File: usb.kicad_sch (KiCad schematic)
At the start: 23 parts, among them J26 FTSH-105-01-L-DV-K, J3 CX90B1-24P, U3 MSPM0G5187SPMR, U8 TPD4E004DRYR, Y4 32.768KHz 12.5pF 20ppm

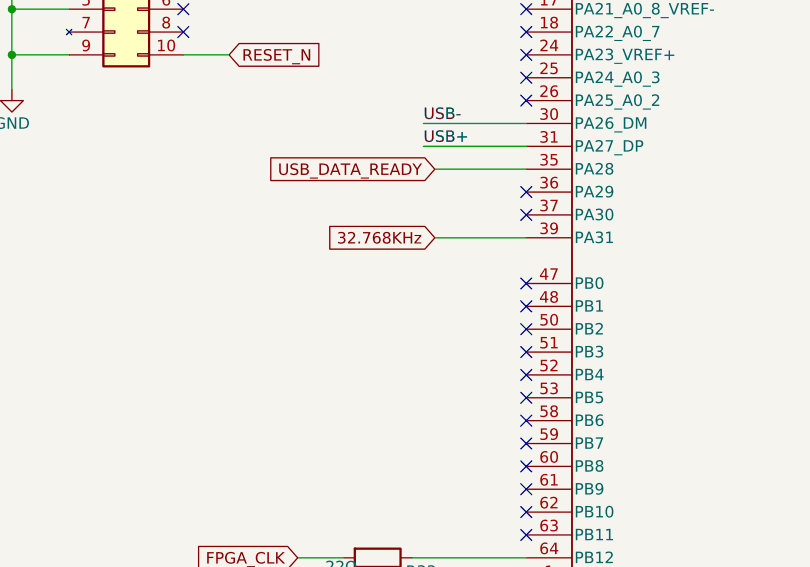
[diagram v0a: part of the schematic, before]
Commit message: Split the USB CPU and main CPU reset lines
Signed-off-by: Corey Minyard <corey@minyard.net>
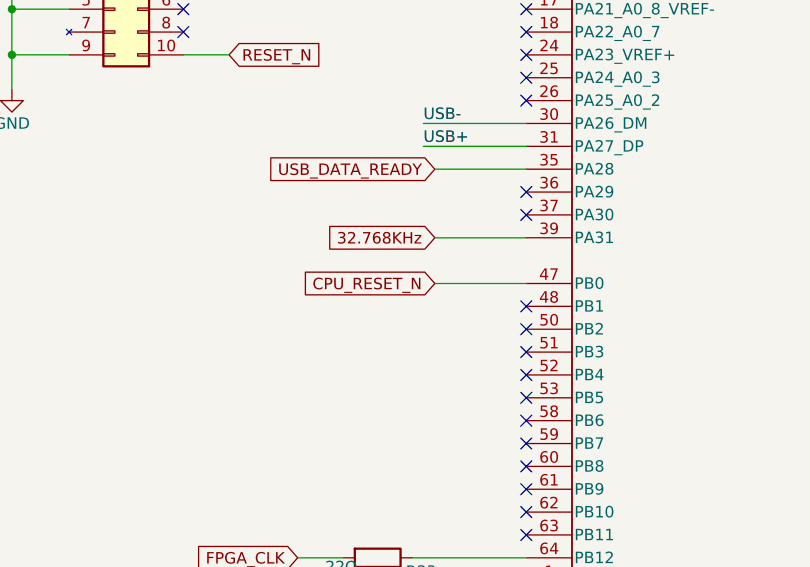
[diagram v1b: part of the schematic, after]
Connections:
- net CPU_RESET_N: now reaches U3.47 (PB0)
- no-connect marks 55 -> 54
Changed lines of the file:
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@@
-	)
-	(no_connect
-		(at 95.25 124.46)
 	)
 	(no_connect
@@
 		(pts
 			(xy 191.77 67.31) (xy 194.31 67.31)
+		)
+		(stroke
+			(width 0)
+			(type default)
+		)
+	)
+	(wire
+		(pts
+			(xy 85.09 124.46) (xy 95.25 124.46)
 		)
 		(stroke
@@
 			(effects
 				(font
+					(size 1.27 1.27)
+				)
+				(justify right)
+				(hide yes)
+			)
+		)
+	)
+	(global_label "CPU_RESET_N"
+		(shape input)
+		(at 85.09 124.46 180)
+		(fields_autoplaced yes)
+		(effects
+			(font
+				(size 1.27 1.27)
+			)
+			(justify right)
+		)
+		(property "Intersheetrefs" "${INTERSHEET_REFS}"
+			(at 69.2235 124.46 0)
+			(effects
+				(font

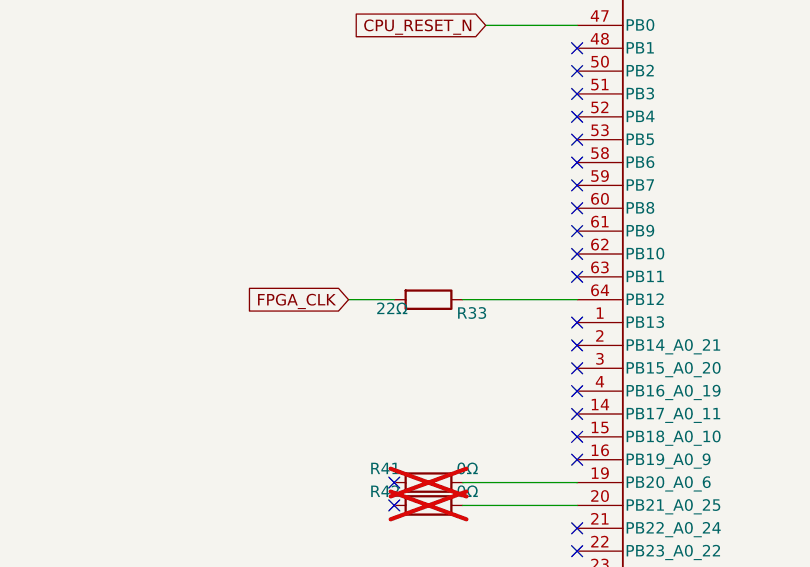
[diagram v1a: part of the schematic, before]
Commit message: Move he FPGA clock to pin 62 on the USB chip
That is easily drivable with PWM, if I can figure out how that works.

Signed-off-by: Corey Minyard <corey@minyard.net>
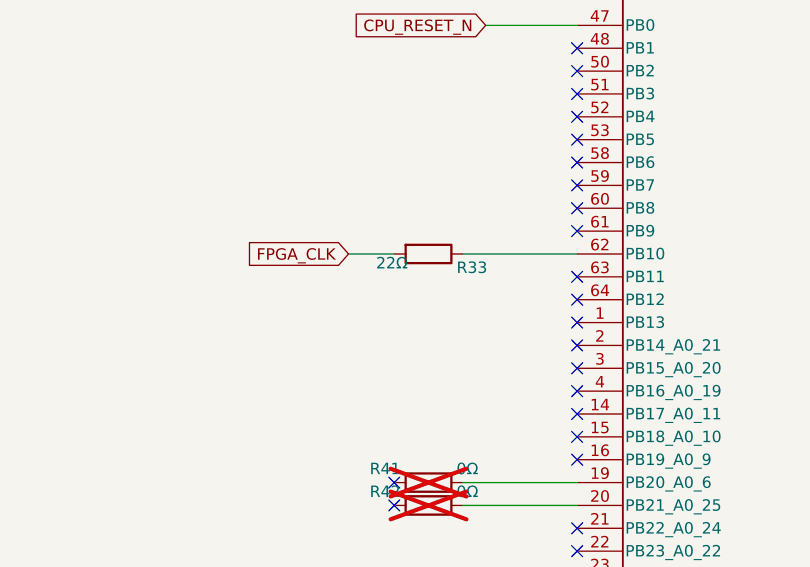
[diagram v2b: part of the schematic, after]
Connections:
- net at R33.1: now also U3.62 (PB10); no longer U3.64 (PB12)
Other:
- moved on the sheet: R33
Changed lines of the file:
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@@
+	)
+	(no_connect
+		(at 95.25 154.94)
 	)
 	(no_connect
@@
 	)
 	(no_connect
-		(at 95.25 149.86)
-	)
-	(no_connect
 		(at 95.25 137.16)
 	)
@@
 	(wire
 		(pts
+			(xy 82.55 149.86) (xy 95.25 149.86)
+		)
+		(stroke
+			(width 0)
+			(type default)
+		)
+	)
+	(wire
+		(pts
 			(xy 248.92 106.68) (xy 182.88 106.68)
 		)
@@
 	(wire
 		(pts
-			(xy 69.85 154.94) (xy 74.93 154.94)
-		)
-		(stroke
-			(width 0)
-			(type default)
-		)
-	)
-	(wire
-		(pts
 			(xy 238.76 85.09) (xy 257.81 85.09)
 		)
@@
 	(wire
 		(pts
+			(xy 69.85 149.86) (xy 74.93 149.86)
+		)
+		(stroke
+			(width 0)
+			(type default)
+		)
+	)
+	(wire
+		(pts
 			(xy 68.58 33.02) (xy 68.58 25.4)
 		)
@@
 		(pts
 			(xy 95.25 50.8) (xy 41.91 50.8)
-		)
-		(stroke
-			(width 0)
-			(type default)
-		)
-	)
-	(wire
-		(pts
-			(xy 82.55 154.94) (xy 95.25 154.94)
 		)
 		(stroke
@@
 		)
 	)
-	(global_label "FPGA_CLK"
-		(shape input)
-		(at 69.85 154.94 180)
-		(fields_autoplaced yes)
-		(effects
-			(font
-				(size 1.27 1.27)
-			)
-			(justify right)
-		)
-		(property "Intersheetrefs" "${INTERSHEET_REFS}"
-			(at 57.6119 154.94 0)
-			(effects
-				(font
-					(size 1.27 1.27)
-				)
-				(justify right)
-				(hide yes)
-			)
-		)
-	)
 	(global_label "USB_VBUS"
 		(shape input)
@@
 		(property "Intersheetrefs" "${INTERSHEET_REFS}"
 			(at 66.0786 111.76 0)
+			(effects
+				(font
+					(size 1.27 1.27)
+				)
+				(justify right)
+				(hide yes)
+			)
+		)
+	)
+	(global_label "FPGA_CLK"
+		(shape input)
+		(at 69.85 149.86 180)
+		(fields_autoplaced yes)
+		(effects
+			(font
+				(size 1.27 1.27)
+			)
+			(justify right)
+		)
+		(property "Intersheetrefs" "${INTERSHEET_REFS}"
+			(at 57.6119 149.86 0)
 			(effects
 				(font
@@
 	(symbol
 		(lib_id "Device:R")
-		(at 78.74 154.94 270)
+		(at 78.74 149.86 270)
 		(unit 1)
 		(exclude_from_sim no)
@@
 		(dnp no)
 		(property "Reference" "R33"
-			(at 83.566 156.464 90)
+			(at 83.566 151.384 90)
 			(effects
 				(font
@@
 		)
 		(property "Value" "22Ω"
-			(at 74.676 155.956 90)
+			(at 74.676 150.876 90)
 			(effects
 				(font
@@
 		)
 		(property "Footprint" "Resistor_SMD:R_0402_1005Metric_Pad0.72x0.64mm_HandSolder"
-			(at 78.74 153.162 90)
+			(at 78.74 148.082 90)
 			(effects
 				(font
@@
 		)
 		(property "Datasheet" "~"
-			(at 78.74 154.94 0)
+			(at 78.74 149.86 0)
 			(effects
 				(font
@@
 		)
 		(property "Description" "Resistor"
-			(at 78.74 154.94 0)
-			(effects
-				(font
+			(at 78.74 149.86 0)
+			(effects
+				(font

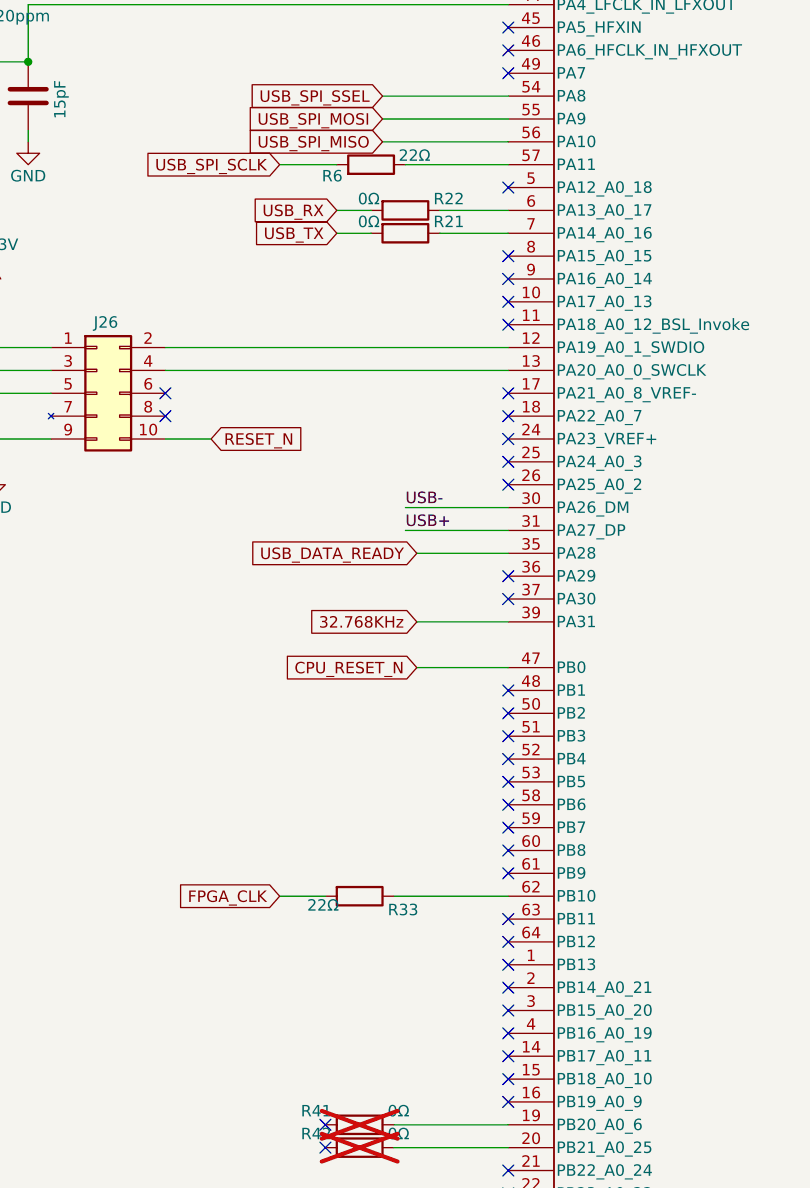
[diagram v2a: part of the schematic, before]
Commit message: Add DNP resistors on the unused pins of the CPU and the USB chip
Move a few things to improve the layout, too.

Signed-off-by: Corey Minyard <corey@minyard.net>
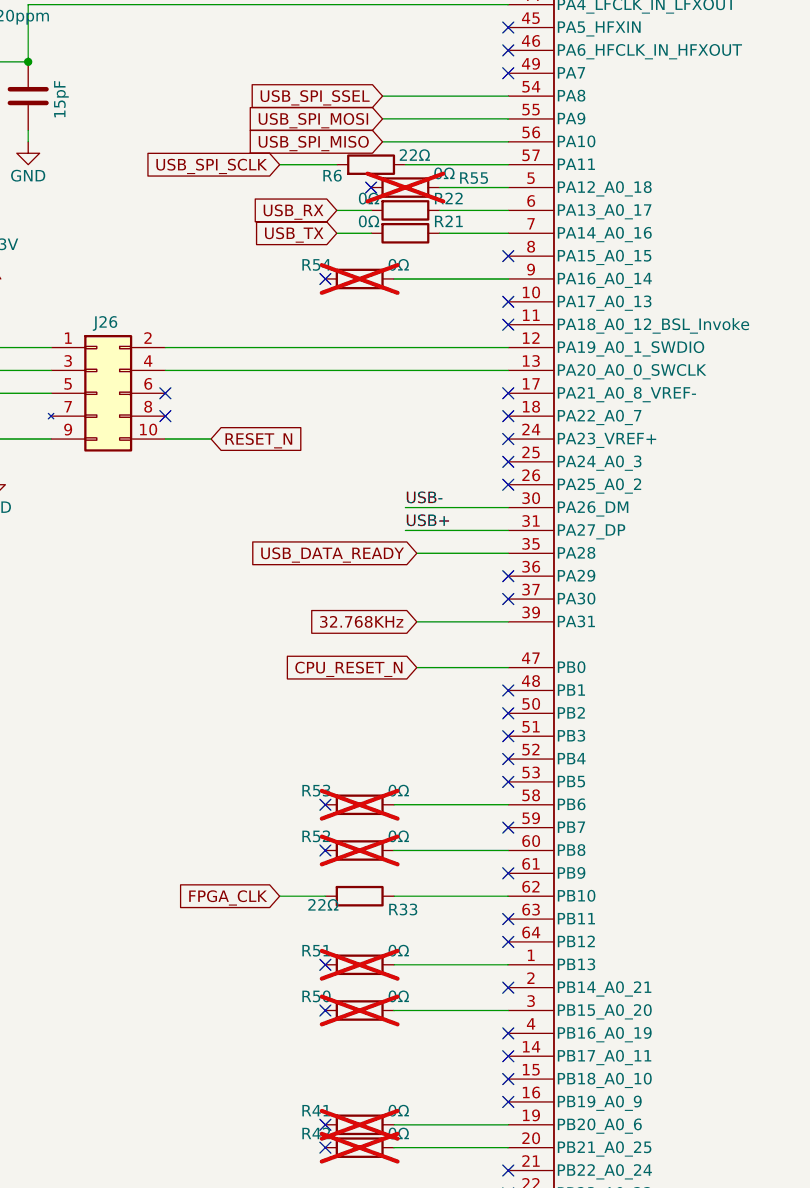
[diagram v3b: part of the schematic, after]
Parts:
- added R50, R51, R52, R53, R54, R55: 0Ω, Resistor_SMD:R_0402_1005Metric, symbol Device:R
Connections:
- net at U3.1 (PB13): now also R51.1
- net at U3.3 (PB15_A0_20): now also R50.1
- net at U3.5 (PA12_A0_18): now also R55.1
- net at U3.58 (PB6): now also R53.1
- net at U3.60 (PB8): now also R52.1
- net at U3.9 (PA16_A0_14): now also R54.1

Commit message: More work
Signed-off-by: Corey Minyard <corey@minyard.net>
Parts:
- R40: value 100KΩ .1% -> 100KΩ 0.1%
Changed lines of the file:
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@@
 			)
 		)
-		(property "Value" "100KΩ  .1%"
+		(property "Value" "100KΩ 0.1%"
 			(at 88.138 43.688 90)
 			(effects
